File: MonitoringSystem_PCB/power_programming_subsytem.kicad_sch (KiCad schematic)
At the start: 12 parts, among them J2 Micro-USB_Conn, Q1 BC817, Q2 BC817, U1 CP2102N-Axx-xQFN28

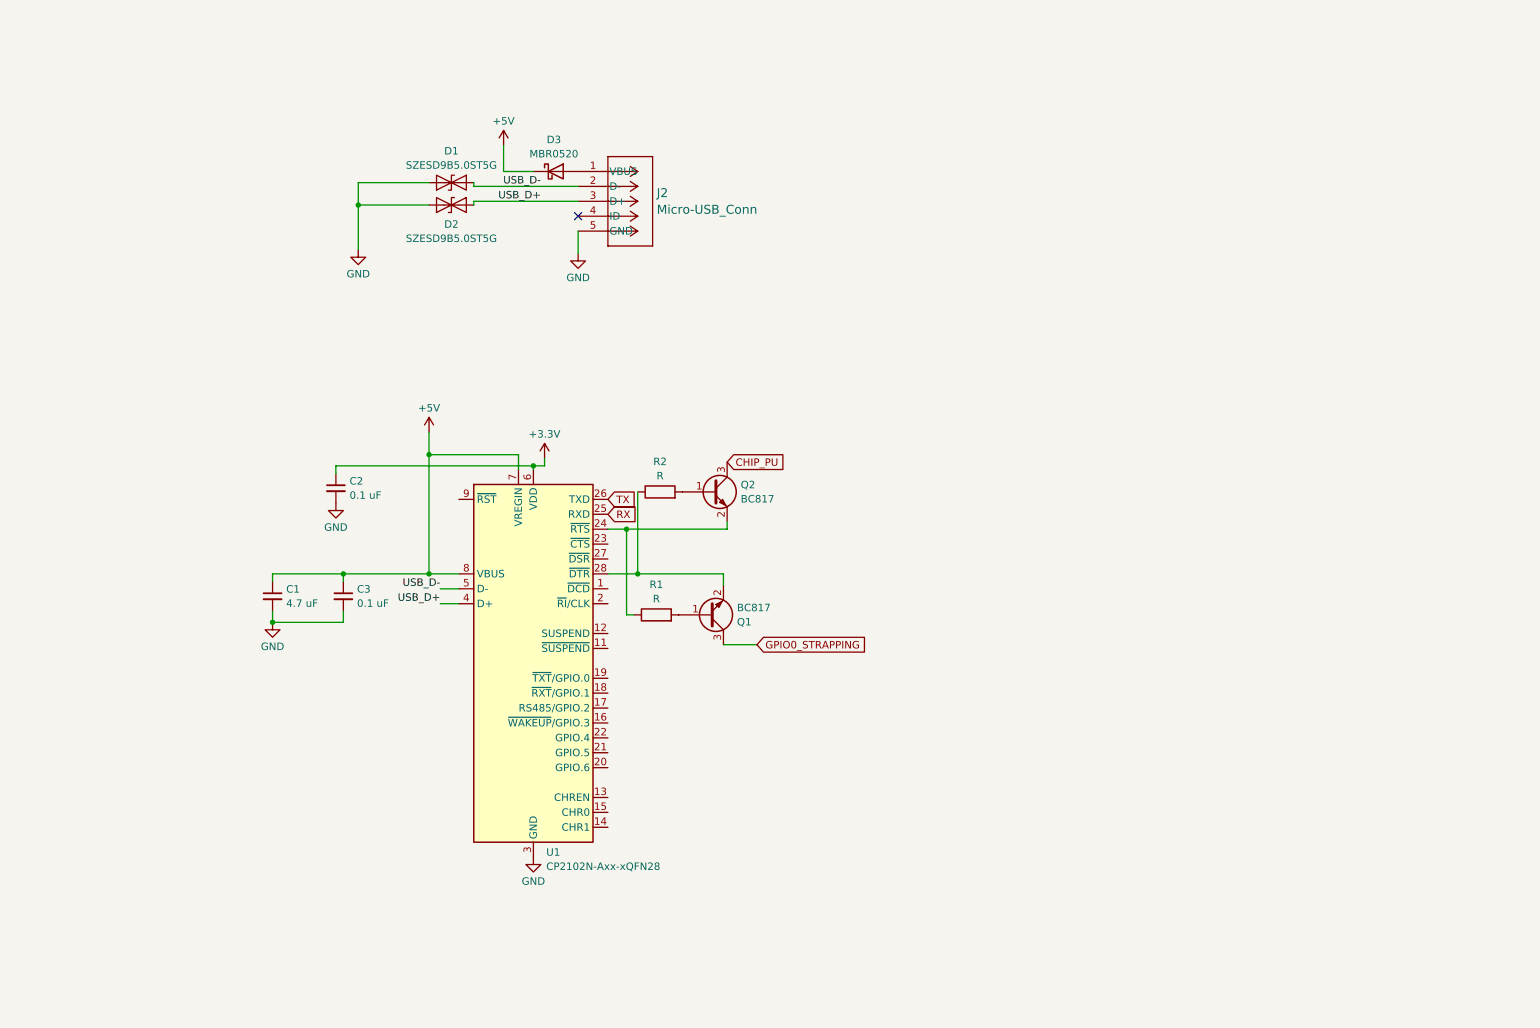
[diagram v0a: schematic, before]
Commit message: finish first draft of schematic of PCB
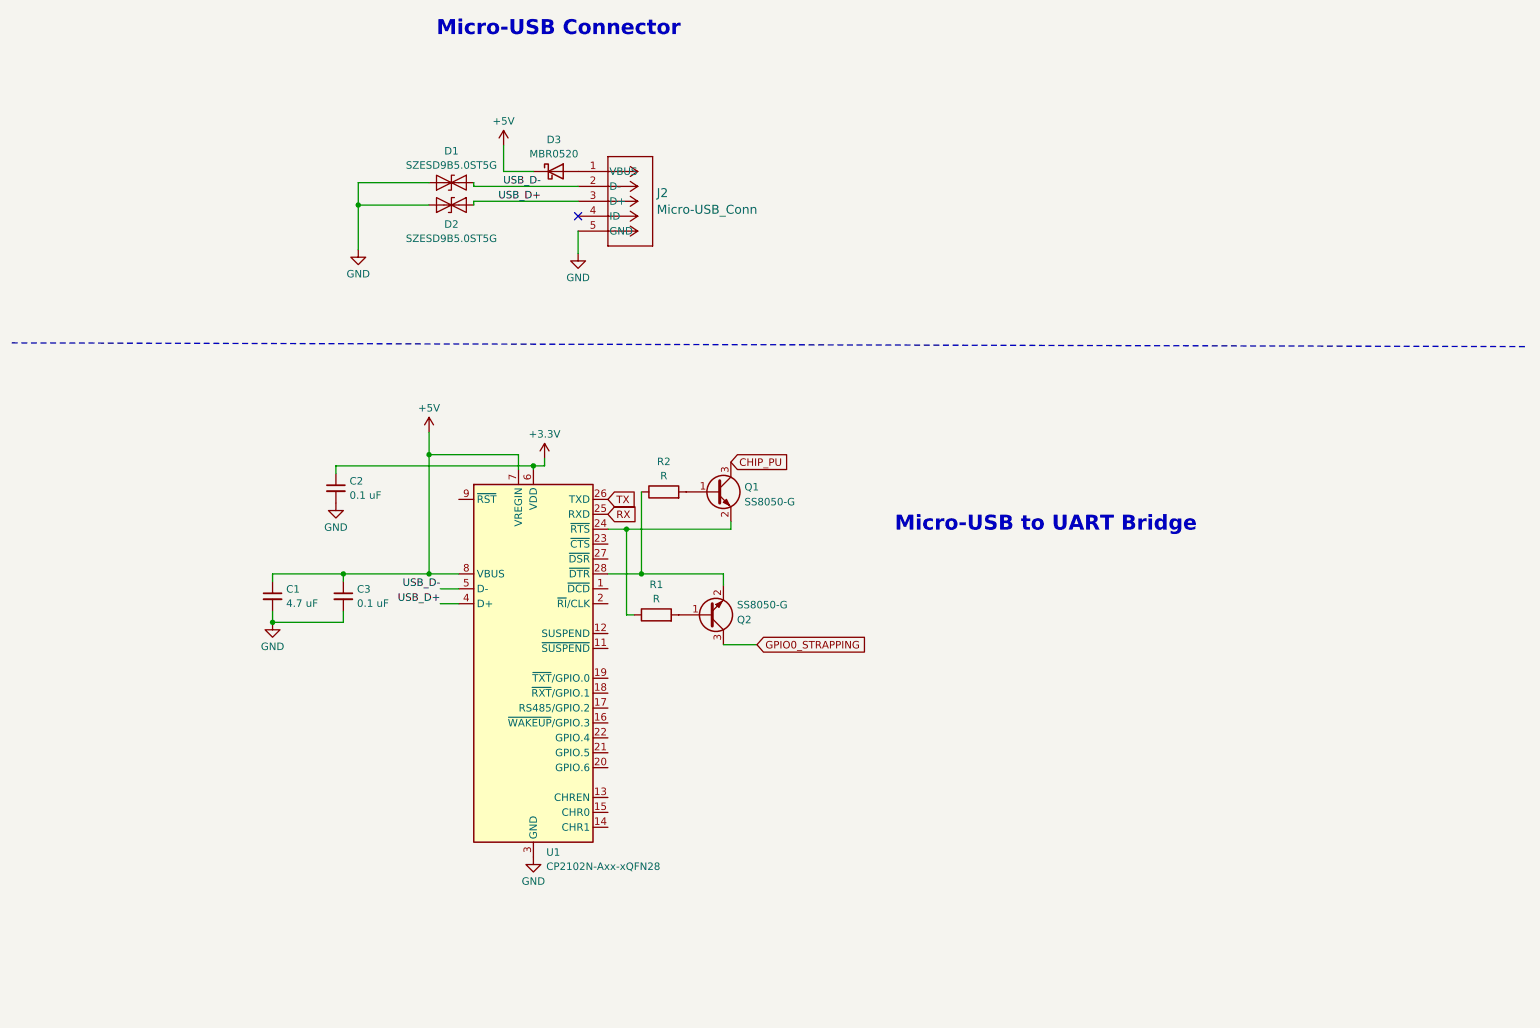
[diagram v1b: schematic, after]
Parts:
- removed Q1, Q2: BC817, Package_TO_SOT_SMD:SOT-23, symbol Transistor_BJT:BC817
- added Q1, Q2: SS8050-G, Package_TO_SOT_SMD:SOT-23, symbol Device:Q_NPN_BEC
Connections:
- net CHIP_PU: now also Q1.3 (C)
- net GPIO0_STRAPPING: now also Q2.3 (C)
- net at R1.1, U1.24 (~{RTS}): now also Q1.2 (E)
- net at R1.2: now also Q2.1 (B)
- net at R2.1, U1.28 (~{DTR}): now also Q2.2 (E)
- net at R2.2: now also Q1.1 (B)
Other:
- note added: "Micro-USB Connector"
- note added: "Micro-USB to UART Bridge"
- moved on the sheet: R2
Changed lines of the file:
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@@
+	)
+	(junction
+		(at 125.095 119.38)
+		(diameter 0)
+		(color 0 0 0 0)
 	)
 	(junction
@@
 	)
 	(junction
-		(at 124.46 119.38)
-		(diameter 0)
-		(color 0 0 0 0)
-	)
-	(junction
 		(at 62.23 127.635)
 		(diameter 0)
@@
 	(wire
 		(pts
-			(xy 124.46 105.41) (xy 124.46 119.38)
+			(xy 125.095 105.41) (xy 125.095 119.38)
 		)
 		(stroke
@@
 		)
 	)
-	(wire
-		(pts
-			(xy 122.555 111.76) (xy 139.7 111.76)
+	(polyline
+		(pts
+			(xy 17.78 80.01) (xy 276.225 80.645)
+		)
+		(stroke
+			(width 0)
+			(type dash)
+		)
+	)
+	(wire
+		(pts
+			(xy 122.555 111.76) (xy 140.335 111.76)
 		)
 		(stroke
@@
 	(wire
 		(pts
-			(xy 139.7 111.76) (xy 139.7 110.49)
+			(xy 140.335 111.76) (xy 140.335 110.49)
 		)
 		(stroke
@@
 	(wire
 		(pts
-			(xy 119.38 119.38) (xy 124.46 119.38)
+			(xy 125.095 119.38) (xy 139.065 119.38)
+		)
+		(stroke
+			(width 0)
+			(type default)
+		)
+	)
+	(wire
+		(pts
+			(xy 119.38 119.38) (xy 125.095 119.38)
 		)
 		(stroke
@@
 	(wire
 		(pts
-			(xy 124.46 119.38) (xy 139.065 119.38)
-		)
-		(stroke
-			(width 0)
-			(type default)
-		)
-	)
-	(wire
-		(pts
 			(xy 74.295 127.635) (xy 62.23 127.635)
 		)
@@
 			(width 0)
 			(type default)
+		)
+	)
+	(text "Micro-USB to UART Bridge"
+		(exclude_from_sim no)
+		(at 168.275 112.395 0)
+		(effects
+			(font
+				(size 2.54 2.54)
+				(thickness 0.762)
+				(bold yes)
+			)
+			(justify left bottom)
+		)
+	)
+	(text "Micro-USB Connector"
+		(exclude_from_sim no)
+		(at 90.17 27.94 0)
+		(effects
+			(font
+				(size 2.54 2.54)
+				(thickness 0.762)
+				(bold yes)
+			)
+			(justify left bottom)
 		)
 	)
@@
 	(global_label "CHIP_PU"
 		(shape input)
-		(at 139.7 100.33 0)
+		(at 140.335 100.33 0)
 		(fields_autoplaced yes)
 		(effects
@@
 		)
 		(property "Intersheetrefs" "${INTERSHEET_REFS}"
-			(at 150.7286 100.33 0)
+			(at 151.3636 100.33 0)
 			(effects
 				(font
@@
 	)
 	(symbol
+		(lib_id "Device:Q_NPN_BEC")
+		(at 136.525 126.365 0)
+		(mirror x)
+		(unit 1)
+		(exclude_from_sim no)
+		(in_bom yes)
+		(on_board yes)
+		(dnp no)
+		(property "Reference" "Q2"
+			(at 141.3764 127.1997 0)
+			(effects
+				(font
+					(size 1.27 1.27)
+				)
+				(justify left)
+			)
+		)
+		(property "Value" "SS8050-G"
+			(at 141.3764 124.6628 0)
+			(effects
+				(font
+					(size 1.27 1.27)
+				)
+				(justify left)
+			)
+		)
+		(property "Footprint" "Package_TO_SOT_SMD:SOT-23"
+			(at 141.605 128.905 0)
+			(effects
+				(font
+					(size 1.27 1.27)
+				)
+				(hide yes)
+			)
+		)
+		(property "Datasheet" "~"
+			(at 136.525 126.365 0)
+			(effects
+				(font
+					(size 1.27 1.27)
+				)
+				(hide yes)
+			)
+		)
+		(property "Description" ""
+			(at 136.525 126.365 0)
+			(effects
+				(font
+					(size 1.27 1.27)
+				)
+				(hide yes)
+			)
+		)
+		(pin "1"
+		)
+		(pin "2"
+		)
+		(pin "3"
+		)
+		(instances
+			(project "MonitoringSystem_PCB"
+				(path "/e63e39d7-6ac0-4ffd-8aa3-1841a4541b55/6009ba97-19f7-4ca6-b0d1-715a2fb0321a"
+					(reference "Q2")
+					(unit 1)
+				)
+			)
+		)
+	)
+	(symbol
 		(lib_id "Diode:SZESD9B5.0ST5G")
 		(at 92.71 56.515 180)
@@
 	)
 	(symbol
+		(lib_id "Device:Q_NPN_BEC")
+		(at 137.795 105.41 0)
+		(unit 1)
+		(exclude_from_sim no)
+		(in_bom yes)
+		(on_board yes)
+		(dnp no)
+		(fields_autoplaced yes)
+		(property "Reference" "Q1"
+			(at 142.6464 104.5753 0)
+			(effects
+				(font
+					(size 1.27 1.27)
+				)
+				(justify left)
+			)
+		)
+		(property "Value" "SS8050-G"
+			(at 142.6464 107.1122 0)
+			(effects
+				(font
+					(size 1.27 1.27)
+				)
+				(justify left)
+			)
+		)
+		(property "Footprint" "Package_TO_SOT_SMD:SOT-23"
+			(at 142.875 102.87 0)
+			(effects
+				(font
+					(size 1.27 1.27)
+				)
+				(hide yes)
+			)
+		)
+		(property "Datasheet" "~"
+			(at 137.795 105.41 0)
+			(effects
+				(font
+					(size 1.27 1.27)
+				)
+				(hide yes)
+			)
+		)
+		(property "Description" ""
+			(at 137.795 105.41 0)
+			(effects
+				(font
+					(size 1.27 1.27)
+				)
+				(hide yes)
+			)
+		)
+		(pin "1"
+		)
+		(pin "2"
+		)
+		(pin "3"
+		)
+		(instances
+			(project "MonitoringSystem_PCB"
+				(path "/e63e39d7-6ac0-4ffd-8aa3-1841a4541b55/6009ba97-19f7-4ca6-b0d1-715a2fb0321a"
+					(reference "Q1")
+					(unit 1)
+				)
+			)
+		)
+	)
+	(symbol
 		(lib_id "Diode:SZESD9B5.0ST5G")
 		(at 92.71 52.705 180)
@@
 	(symbol
 		(lib_id "Device:R")
-		(at 128.27 105.41 90)
+		(at 128.905 105.41 90)
 		(unit 1)
 		(exclude_from_sim no)
@@
 		(fields_autoplaced yes)
 		(property "Reference" "R2"
-			(at 128.27 100.2495 90)
+			(at 128.905 100.2495 90)
 			(effects
 				(font
@@
 		)
 		(property "Value" "R"
-			(at 128.27 102.6738 90)
+			(at 128.905 102.6738 90)
 			(effects
 				(font
@@
 		)
 		(property "Footprint" ""
-			(at 128.27 107.188 90)
+			(at 128.905 107.188 90)
 			(effects
 				(font
@@
 		)
 		(property "Datasheet" "~"
-			(at 128.27 105.41 0)
+			(at 128.905 105.41 0)
 			(effects
 				(font
@@
 		)
 		(property "Description" "Resistor"
-			(at 128.27 105.41 0)
+			(at 128.905 105.41 0)
 			(effects
 				(font
@@
 	)
 	(symbol
-		(lib_id "Transistor_BJT:BC817")
-		(at 136.525 126.365 0)
-		(mirror x)
-		(unit 1)
-		(exclude_from_sim no)
-		(in_bom yes)
-		(on_board yes)
-		(dnp no)
-		(property "Reference" "Q1"
-			(at 141.3764 127.5772 0)
-			(effects
-				(font
-					(size 1.27 1.27)
-				)
-				(justify left)
-			)
-		)
-		(property "Value" "BC817"
-			(at 141.3764 125.1529 0)
-			(effects
-				(font
-					(size 1.27 1.27)
-				)
-				(justify left)
-			)
-		)
-		(property "Footprint" "Package_TO_SOT_SMD:SOT-23"
-			(at 141.605 124.46 0)
-			(effects
-				(font
-					(size 1.27 1.27)
-					(italic yes)
-				)
-				(justify left)
-				(hide yes)
-			)
-		)
-		(property "Datasheet" "https://www.onsemi.com/pub/Collateral/BC818-D.pdf"
-			(at 136.525 126.365 0)
-			(effects
-				(font
-					(size 1.27 1.27)
-				)
-				(justify left)
-				(hide yes)
-			)
-		)
-		(property "Description" "0.8A Ic, 45V Vce, NPN Transistor, SOT-23"
-			(at 136.525 126.365 0)
-			(effects
-				(font
-					(size 1.27 1.27)
-				)
-				(hide yes)
-			)
-		)
-		(pin "2"
-		)
-		(pin "3"
-		)
-		(pin "1"
-		)
-		(instances
-			(project "MonitoringSystem_PCB"
-				(path "/e63e39d7-6ac0-4ffd-8aa3-1841a4541b55/6009ba97-19f7-4ca6-b0d1-715a2fb0321a"
-					(reference "Q1")
-					(unit 1)
-				)
-			)
-		)
-	)
-	(symbol
 		(lib_id "power:+5V")
 		(at 88.9 95.25 0)
@@
 					(unit 1)
 				)
-			)
-		)
-	)
-	(symbol
-		(lib_id "Transistor_BJT:BC817")
-		(at 137.16 105.41 0)
-		(unit 1)
-		(exclude_from_sim no)
-		(in_bom yes)
-		(on_board yes)
-		(dnp no)
-		(fields_autoplaced yes)
-		(property "Reference" "Q2"
-			(at 142.0114 104.1978 0)
-			(effects
-				(font
-					(size 1.27 1.27)
-				)
-				(justify left)
-			)
-		)
-		(property "Value" "BC817"
-			(at 142.0114 106.6221 0)
-			(effects
-				(font
-					(size 1.27 1.27)
-				)
-				(justify left)
-			)
-		)
-		(property "Footprint" "Package_TO_SOT_SMD:SOT-23"
-			(at 142.24 107.315 0)
-			(effects
-				(font
-					(size 1.27 1.27)
-					(italic yes)
-				)
-				(justify left)
-				(hide yes)
-			)
-		)
-		(property "Datasheet" "https://www.onsemi.com/pub/Collateral/BC818-D.pdf"
-			(at 137.16 105.41 0)
-			(effects
-				(font
-					(size 1.27 1.27)
-				)
-				(justify left)
-				(hide yes)
-			)
-		)
-		(property "Description" "0.8A Ic, 45V Vce, NPN Transistor, SOT-23"
-			(at 137.16 105.41 0)
-			(effects
-				(font
-					(size 1.27 1.27)
-				)
-				(hide yes)
-			)
-		)
-		(pin "2"
-		)
-		(pin "3"
-		)
-		(pin "1"
-		)
-		(instances
-			(project "MonitoringSystem_PCB"
-				(path "/e63e39d7-6ac0-4ffd-8aa3-1841a4541b55/6009ba97-19f7-4ca6-b0d1-715a2fb0321a"
-					(reference "Q2")
-					(unit 1)
-				)

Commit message: switched micro-usb for usb-b, started pcb
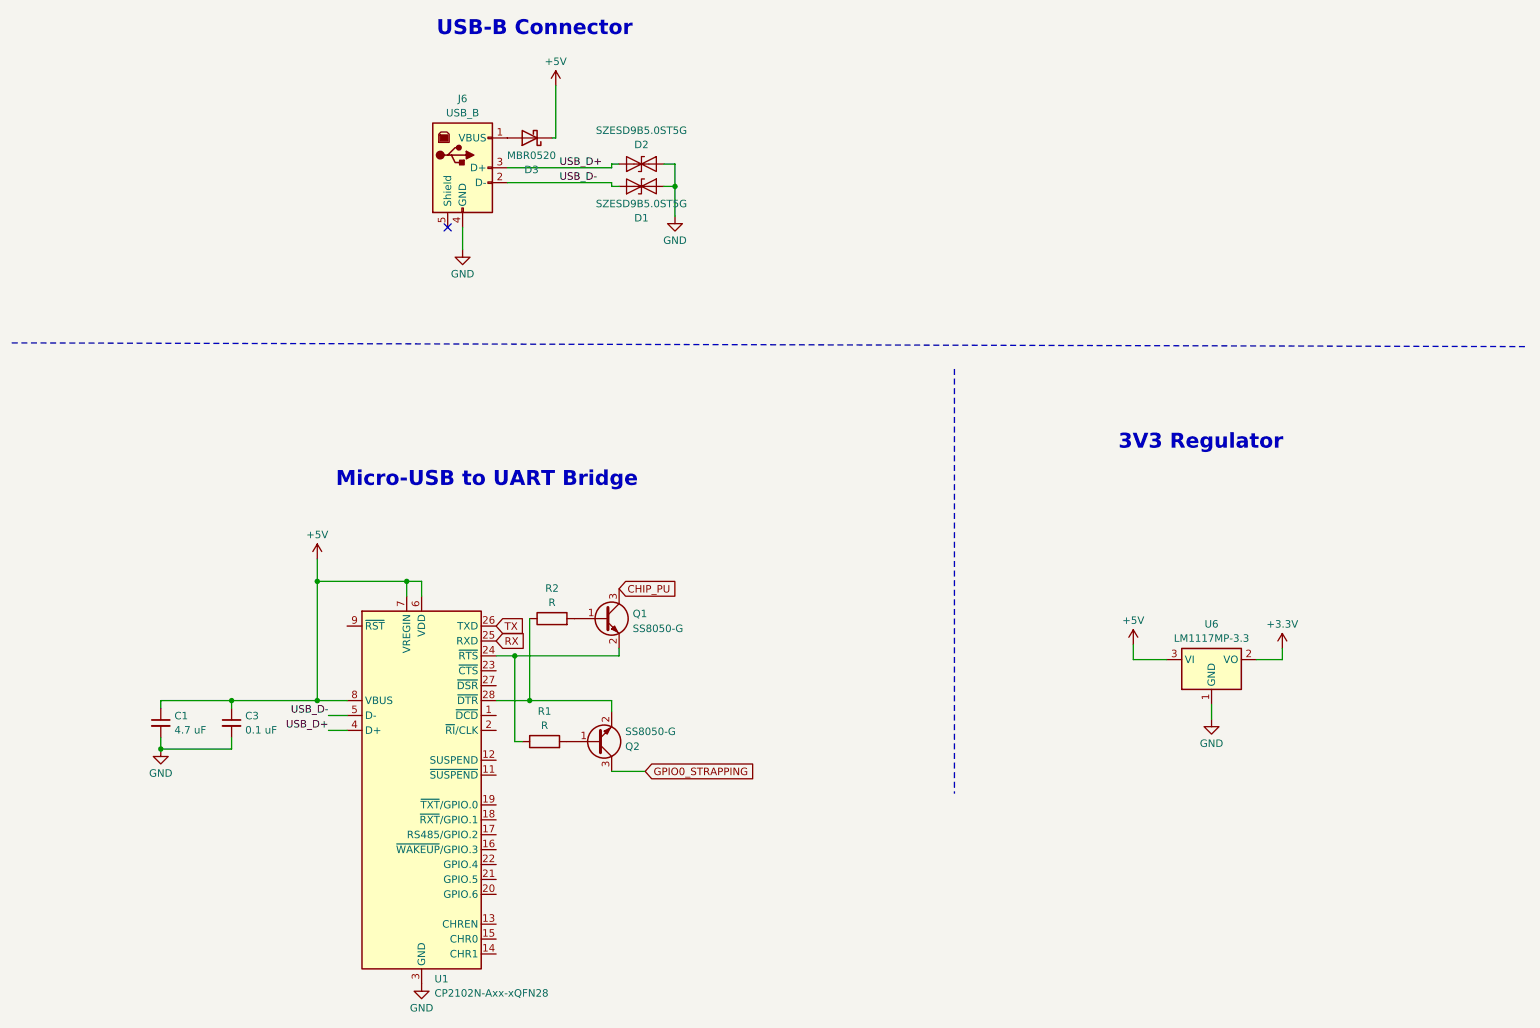
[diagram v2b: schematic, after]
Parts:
- removed C2: 0.1 uF, symbol Device:C_Small
- removed J2: Micro-USB_Conn, CON00679_5_MOL, symbol micro-usb_connector:1050171001
- added J6: USB_B, USB-B:CUI_UJ2-BH-W1-TH, symbol Connector:USB_B
- added U6: LM1117MP-3.3, Package_TO_SOT_SMD:SOT-223-3_TabPin2, symbol Regulator_Linear:LM1117MP-3.3
- C1, C3: footprint (none) -> Capacitor_SMD:C_0805_2012Metric
- R1, R2: footprint (none) -> Resistor_SMD:R_0805_2012Metric
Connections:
- net +3.3V: now also U6.2 (VO); no longer U1.6 (VDD)
- net +5V: now also U1.6 (VDD), U6.3 (VI)
- net GND: now also J6.4 (GND), U6.1 (GND)
- net USB_D+: now also J6.3 (D+)
- net USB_D-: now also J6.2 (D-)
- net at D3.2 (A): now also J6.1 (VBUS)
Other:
- note added: "3V3 Regulator"
- note added: "USB-B Connector"
- note removed: "Micro-USB Connector"
- moved on the sheet: C1, C3, D1, D2, D3, Q1, Q2, R1, R2, U1
